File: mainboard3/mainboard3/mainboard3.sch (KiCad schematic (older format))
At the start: 27 parts, among them J0 Conn_01x18, J1 Conn_01x18, J2 Conn_01x18, J4 Conn_01x18, J5 Conn_01x18, T0 Screw_Terminal_01x06, T1 Screw_Terminal_01x06, T10 Screw_Terminal_01x06, T11 Screw_Terminal_01x06, T12 Screw_Terminal_01x06, T2 Screw_Terminal_01x06, T3 Screw_Terminal_01x06, T4 Screw_Terminal_01x06, T5 Screw_Terminal_01x06, T6 Screw_Terminal_01x06, T7 Screw_Terminal_01x06, T8 Screw_Terminal_01x06, T9 Screw_Terminal_01x06, U1 STM32_F4xx, U2 ModuleINA3221, U3 ModuleINA3221, U4 ModuleINA3221, U5 ModuleINA3221, U6 ULN2803A, U7 ULN2803A, X1 Screw_Terminal_01x04

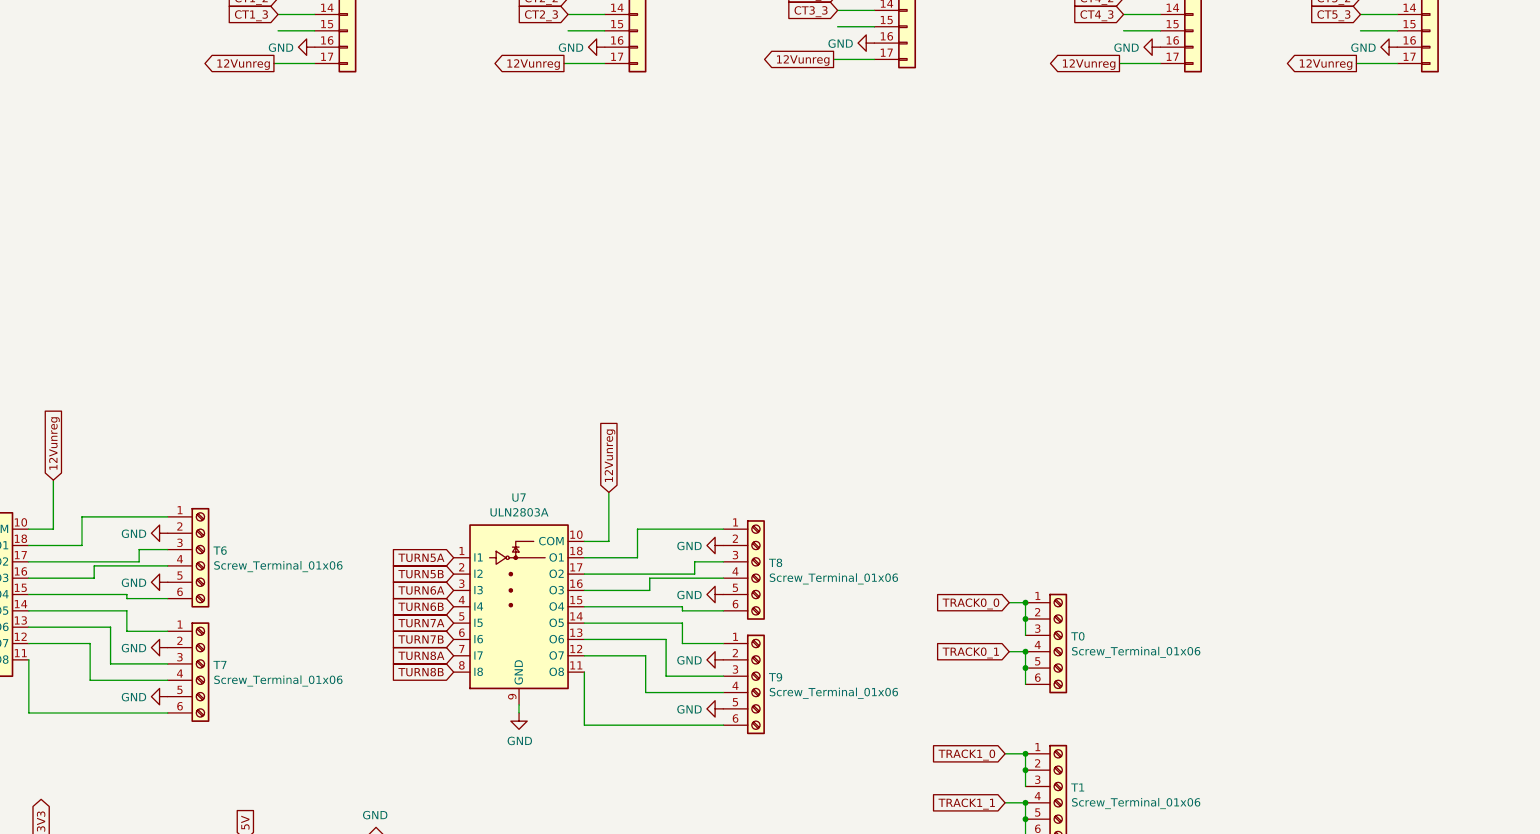
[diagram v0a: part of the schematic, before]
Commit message: adding CAN interface
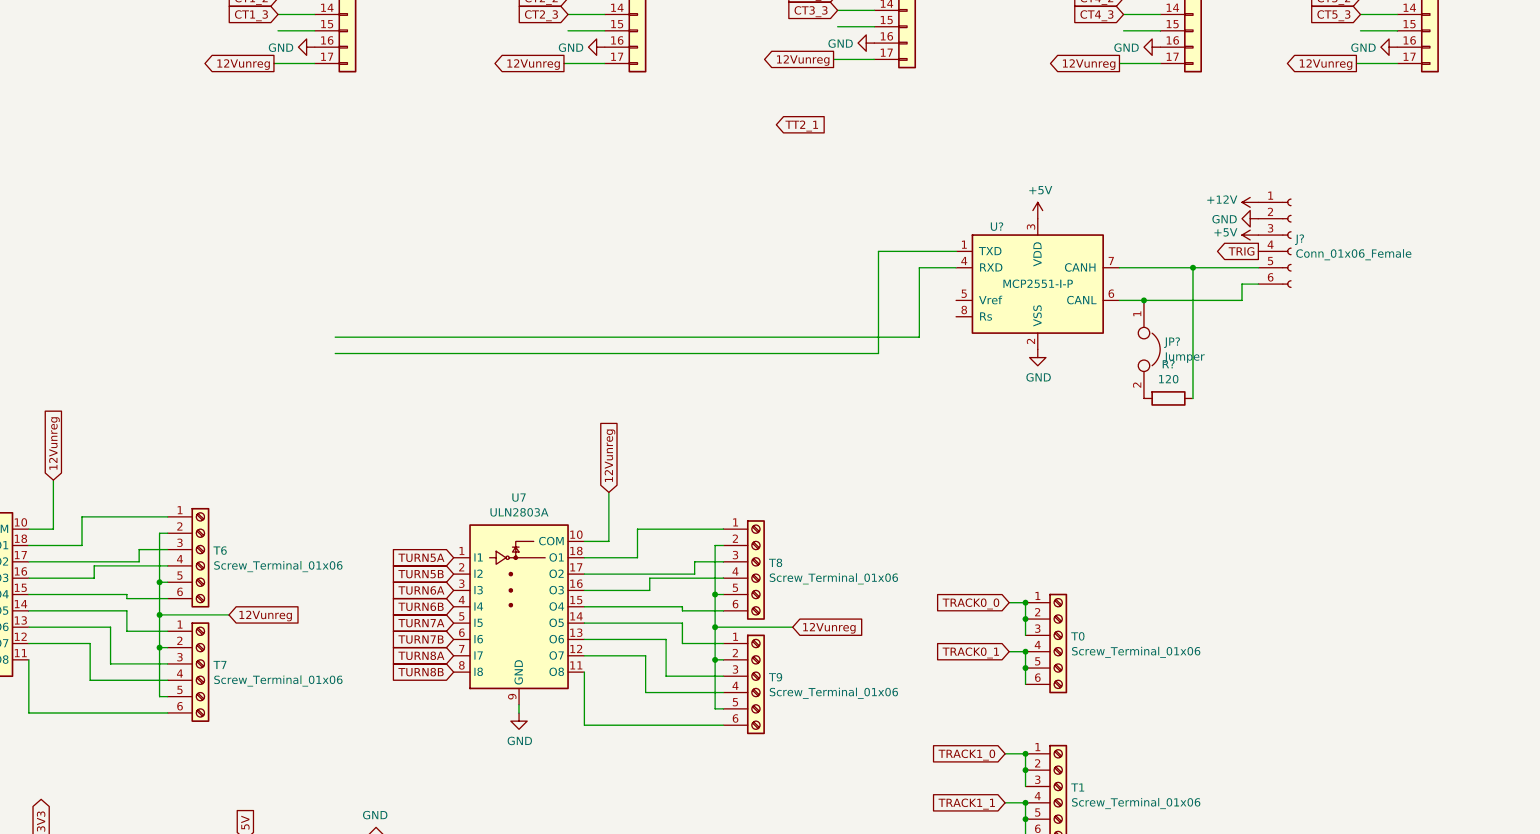
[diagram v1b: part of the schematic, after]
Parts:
- added J?: Conn_01x06_Female, Connector_PinHeader_2.54mm:PinHeader_1x06_P2.54mm_Vertical, symbol Connector:Conn_01x06_Female
- added JP?: Jumper, Connector_PinHeader_2.54mm:PinHeader_1x02_P2.54mm_Vertical, symbol Device:Jumper
- added R?: 120, Resistor_THT:R_Axial_DIN0207_L6.3mm_D2.5mm_P7.62mm_Horizontal, symbol Device:R
- added U?: MCP2551-I-P, Package_DIP:DIP-8_W7.62mm, symbol Interface_CAN_LIN:MCP2551-I-P
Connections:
- net labels added: +12V, +5V, TRIG, TT2_1
- wire segments 201 -> 232
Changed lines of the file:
@@
 Wire Wire Line
 	2350 6550 2350 6225
-$Comp
-L power:GND #PWR0112
-U 1 1 60F13817
-P 3200 5450
-F 0 "#PWR0112" H 3200 5200 50  0001 C CNN
-F 1 "GND" V 3205 5322 50  0000 R CNN
-F 2 "" H 3200 5450 50  0001 C CNN
-F 3 "" H 3200 5450 50  0001 C CNN
-	1    3200 5450
-	0    1    1    0
-$EndComp
-$Comp
-L power:GND #PWR0113
-U 1 1 60F13F45
-P 3200 5750
-F 0 "#PWR0113" H 3200 5500 50  0001 C CNN
-F 1 "GND" V 3205 5622 50  0000 R CNN
-F 2 "" H 3200 5750 50  0001 C CNN
-F 3 "" H 3200 5750 50  0001 C CNN
-	1    3200 5750
-	0    1    1    0
-$EndComp
-$Comp
-L power:GND #PWR0114
-U 1 1 60F1440A
-P 3200 6150
-F 0 "#PWR0114" H 3200 5900 50  0001 C CNN
-F 1 "GND" V 3205 6022 50  0000 R CNN
-F 2 "" H 3200 6150 50  0001 C CNN
-F 3 "" H 3200 6150 50  0001 C CNN
-	1    3200 6150
-	0    1    1    0
-$EndComp
-$Comp
-L power:GND #PWR0115
-U 1 1 60F14973
-P 3200 6450
-F 0 "#PWR0115" H 3200 6200 50  0001 C CNN
-F 1 "GND" V 3205 6322 50  0000 R CNN
-F 2 "" H 3200 6450 50  0001 C CNN
-F 3 "" H 3200 6450 50  0001 C CNN
-	1    3200 6450
-	0    1    1    0
-$EndComp
 Text GLabel 2500 5125 1    50   Input ~ 0
 12Vunreg
@@
 Wire Wire Line
 	5750 6625 5750 6300
-$Comp
-L power:GND #PWR0118
-U 1 1 6108F63E
-P 6600 5525
-F 0 "#PWR0118" H 6600 5275 50  0001 C CNN
-F 1 "GND" V 6605 5397 50  0000 R CNN
-F 2 "" H 6600 5525 50  0001 C CNN
-F 3 "" H 6600 5525 50  0001 C CNN
-	1    6600 5525
-	0    1    1    0
-$EndComp
-$Comp
-L power:GND #PWR0119
-U 1 1 6108F644
-P 6600 5825
-F 0 "#PWR0119" H 6600 5575 50  0001 C CNN
-F 1 "GND" V 6605 5697 50  0000 R CNN
-F 2 "" H 6600 5825 50  0001 C CNN
-F 3 "" H 6600 5825 50  0001 C CNN
-	1    6600 5825
-	0    1    1    0
-$EndComp
-$Comp
-L power:GND #PWR0120
-U 1 1 6108F64A
-P 6600 6225
-F 0 "#PWR0120" H 6600 5975 50  0001 C CNN
-F 1 "GND" V 6605 6097 50  0000 R CNN
-F 2 "" H 6600 6225 50  0001 C CNN
-F 3 "" H 6600 6225 50  0001 C CNN
-	1    6600 6225
-	0    1    1    0
-$EndComp
-$Comp
-L power:GND #PWR0121
-U 1 1 6108F650
-P 6600 6525
-F 0 "#PWR0121" H 6600 6275 50  0001 C CNN
-F 1 "GND" V 6605 6397 50  0000 R CNN
-F 2 "" H 6600 6525 50  0001 C CNN
-F 3 "" H 6600 6525 50  0001 C CNN
-	1    6600 6525
-	0    1    1    0
-$EndComp
 Text GLabel 5900 5200 1    50   Input ~ 0
 12Vunreg
@@
 Wire Wire Line
 	3950 13825 4200 13825
+Wire Wire Line
+	3150 6150 3200 6150
+Wire Wire Line
+	3150 6150 3150 5950
+Wire Wire Line
+	3150 5750 3200 5750
+Connection ~ 3150 6150
+Wire Wire Line
+	3150 5750 3150 5450
+Wire Wire Line
+	3150 5450 3200 5450
+Connection ~ 3150 5750
+Wire Wire Line
+	3200 6450 3150 6450
+Wire Wire Line
+	3150 6150 3150 6450
+Wire Wire Line
+	3150 5950 3575 5950
+Connection ~ 3150 5950
+Wire Wire Line
+	3150 5950 3150 5750
+Text GLabel 3575 5950 2    50   Input ~ 0
+12Vunreg
+Wire Wire Line
+	6600 5525 6550 5525
+Wire Wire Line
+	6550 5525 6550 5825
+Wire Wire Line
+	6550 5825 6600 5825
+Wire Wire Line
+	6550 5825 6550 6025
+Wire Wire Line
+	6550 6225 6600 6225
+Connection ~ 6550 5825
+Wire Wire Line
+	6550 6225 6550 6525
+Wire Wire Line
+	6550 6525 6600 6525
+Connection ~ 6550 6225
+Wire Wire Line
+	6550 6025 7025 6025
+Connection ~ 6550 6025
+Wire Wire Line
+	6550 6025 6550 6225
+Text GLabel 7025 6025 2    50   Input ~ 0
+12Vunreg
+$Comp
+L Interface_CAN_LIN:MCP2551-I-P U?
+U 1 1 61B9B58C
+P 8525 3925
+F 0 "U?" H 8275 4275 50  0000 C CNN
+F 1 "MCP2551-I-P" H 8525 3925 50  0000 C CNN
+F 2 "Package_DIP:DIP-8_W7.62mm" H 8525 3425 50  0001 C CIN
+F 3 "http://ww1.microchip.com/downloads/en/devicedoc/21667d.pdf" H 8525 3925 50  0001 C CNN
+	1    8525 3925
+	1    0    0    -1
+$EndComp
+$Comp
+L Device:Jumper JP?
+U 1 1 61B9B592
+P 9175 4325
+F 0 "JP?" V 9129 4452 50  0000 L CNN
+F 1 "Jumper" V 9220 4452 50  0000 L CNN
+F 2 "Connector_PinHeader_2.54mm:PinHeader_1x02_P2.54mm_Vertical" H 9175 4325 50  0001 C CNN
+F 3 "~" H 9175 4325 50  0001 C CNN
+	1    9175 4325
+	0    1    1    0
+$EndComp
+$Comp
+L Device:R R?
+U 1 1 61B9B598
+P 9325 4625
+F 0 "R?" V 9118 4625 50  0000 C CNN
+F 1 "120" V 9209 4625 50  0000 C CNN
+F 2 "Resistor_THT:R_Axial_DIN0207_L6.3mm_D2.5mm_P7.62mm_Horizontal" V 9255 4625 50  0001 C CNN
+F 3 "~" H 9325 4625 50  0001 C CNN
+	1    9325 4625
+	0    1    1    0
+$EndComp
+Wire Wire Line
+	9025 4025 9175 4025
+Connection ~ 9175 4025
+Wire Wire Line
+	9025 3825 9475 3825
+Connection ~ 9475 3825
+$Comp
+L power:GND #PWR?
+U 1 1 61B9B5A2
+P 8525 4325
+F 0 "#PWR?" H 8525 4075 50  0001 C CNN
+F 1 "GND" H 8530 4152 50  0000 C CNN
+F 2 "" H 8525 4325 50  0001 C CNN
+F 3 "" H 8525 4325 50  0001 C CNN
+	1    8525 4325
+	1    0    0    -1
+$EndComp
+Wire Wire Line
+	9475 3825 9475 4625
+$Comp
+L power:+5V #PWR?
+U 1 1 61B9B5A9
+P 8525 3525
+F 0 "#PWR?" H 8525 3375 50  0001 C CNN
+F 1 "+5V" H 8540 3698 50  0000 C CNN
+F 2 "" H 8525 3525 50  0001 C CNN
+F 3 "" H 8525 3525 50  0001 C CNN
+	1    8525 3525
+	1    0    0    -1
+$EndComp
+Wire Wire Line
+	9475 3825 9875 3825
+Wire Wire Line
+	9875 3925 9775 3925
+Wire Wire Line
+	9775 3925 9775 4025
+Wire Wire Line
+	9175 4025 9775 4025
+$Comp
+L power:GND #PWR?
+U 1 1 61B9B5B3
+P 9875 3525
+F 0 "#PWR?" H 9875 3275 50  0001 C CNN
+F 1 "GND" V 9880 3397 50  0000 R CNN
+F 2 "" H 9875 3525 50  0001 C CNN
+F 3 "" H 9875 3525 50  0001 C CNN
+	1    9875 3525
+	0    1    1    0
+$EndComp
+$Comp
+L power:+5V #PWR?
+U 1 1 61B9B5B9
+P 9875 3625
+F 0 "#PWR?" H 9875 3475 50  0001 C CNN
+F 1 "+5V" V 9890 3753 50  0000 L CNN
+F 2 "" H 9875 3625 50  0001 C CNN
+F 3 "" H 9875 3625 50  0001 C CNN
+	1    9875 3625
+	0    -1   -1   0
+$EndComp
+$Comp
+L Connector:Conn_01x06_Female J?
+U 1 1 61B9B5BF
+P 10075 3625
+F 0 "J?" H 10103 3601 50  0000 L CNN
+F 1 "Conn_01x06_Female" H 10103 3510 50  0000 L CNN
+F 2 "Connector_PinHeader_2.54mm:PinHeader_1x06_P2.54mm_Vertical" H 10075 3625 50  0001 C CNN
+F 3 "~" H 10075 3625 50  0001 C CNN
+	1    10075 3625
+	1    0    0    -1
+$EndComp
+$Comp
+L power:+12V #PWR?
+U 1 1 61B9B5C5
+P 9875 3425
+F 0 "#PWR?" H 9875 3275 50  0001 C CNN
+F 1 "+12V" V 9890 3553 50  0000 L CNN
+F 2 "" H 9875 3425 50  0001 C CNN
+F 3 "" H 9875 3425 50  0001 C CNN
+	1    9875 3425
+	0    -1   -1   0
+$EndComp
+Text GLabel 9875 3725 0    50   Output ~ 0
+TRIG
+Text GLabel 6925 2950 2    50   Input ~ 0
+TT2_1
+Wire Wire Line
+	4225 4350 7550 4350
+Wire Wire Line
+	7550 4350 7550 3725
+Wire Wire Line
+	7550 3725 8025 3725
+Wire Wire Line
+	4225 4250 7800 4250
+Wire Wire Line
+	7800 4250 7800 3825
+Wire Wire Line
+	7800 3825 8025 3825
 $EndSCHEMATC

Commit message: mainboard3 again
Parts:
- removed T0, T1, T12, T2, T3, T4: Screw_Terminal_01x06, Connector_PinHeader_2.54mm:PinHeader_1x06_P2.54mm_Vertical, symbol Connector:Screw_Terminal_01x06
- added 10k1, R1, R20, R21, R22, R23, R24, R25, R26, R27: R, Resistor_THT:R_Axial_DIN0207_L6.3mm_D2.5mm_P7.62mm_Horizontal, symbol Device:R
- added C1, C2, C3, C4, C5: 100nF, Capacitor_THT:C_Disc_D3.4mm_W2.1mm_P2.50mm, symbol Device:C
- added C6: 0.1µF, Capacitor_THT:C_Disc_D3.4mm_W2.1mm_P2.50mm, symbol Device:CP
- added C7: 10µF, Capacitor_THT:CP_Radial_Tantal_D5.0mm_P2.50mm, symbol Device:CP
- added J7: Conn_01x02_Female, Connector_PinHeader_2.54mm:PinHeader_1x02_P2.54mm_Vertical, symbol Connector:Conn_01x02_Female
- added JG2, JG3, JG4, JG5: Conn_01x03_Female, Connector_PinHeader_2.54mm:PinHeader_1x03_P2.54mm_Vertical, symbol Connector:Conn_01x03_Female
- added JI2, JI3, JI4, JI5: Conn_01x06_Female, Connector_PinHeader_2.54mm:PinHeader_1x06_P2.54mm_Vertical, symbol Connector:Conn_01x06_Female
- added JLED1, JLED2: Conn_01x08_Female, Connector_PinHeader_2.54mm:PinHeader_1x08_P2.54mm_Vertical, symbol Connector:Conn_01x08_Female
- added JT_0_1, JT_0_2, JT_0_3, JT_1_1, JT_1_2, JT_1_3, JT_2_1, JT_2_2, JT_3_1, JT_3_2, JT_4_1, JT_5_1: Screw_Terminal_01x02, Connector_PinHeader_2.54mm:PinHeader_1x02_P2.54mm_Vertical, symbol Connector:Screw_Terminal_01x02
- added R10, R11, R12, R13, R14, R15, R16, R17, R18, R19, R3, R4, R5, R6, R7, R8, R9: 10k, Resistor_THT:R_Axial_DIN0207_L6.3mm_D2.5mm_P7.62mm_Horizontal, symbol Device:R
- added R28: 510, Resistor_THT:R_Axial_DIN0207_L6.3mm_D2.5mm_P7.62mm_Horizontal, symbol Device:R
- added R29: 200, Resistor_THT:R_Axial_DIN0207_L6.3mm_D2.5mm_P7.62mm_Horizontal, symbol Device:R
- added R30: 240, Resistor_THT:R_Axial_DIN0207_L6.3mm_D2.5mm_P7.62mm_Horizontal, symbol Device:R
- added SW1: SW_DIP_x01, Connector_PinHeader_2.54mm:PinHeader_1x02_P2.54mm_Vertical, symbol Switch:SW_DIP_x01
- added U10: LM317_TO220, Package_TO_SOT_THT:TO-220-3_Vertical, symbol Regulator_Linear:LM317_TO-220
- added U9: ULN2803A, Package_DIP:DIP-18_W7.62mm, symbol Transistor_Array:ULN2803A
- gave numbers to parts that had none: 4
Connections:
- net labels added: BOARD_LED, BOARD_LED2, CAN_RX, CAN_TX, I10A, I10B, I11A, I11B, I12A, I12B, I1A, I1B, I2A, I2B, I3A, I3B, I4A, I4B, I5A, I5B, I6A, I6B, I7A, I7B, I8A, I8B, I9A, I9B, LED3, LED4, LED5, LED6, LED7, LED8, V5
- wire segments 232 -> 353
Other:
- moved on the sheet: U3, U4, U5

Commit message: mainboard3  routing
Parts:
- removed JLED1, JLED2: Conn_01x08_Female, Connector_PinHeader_2.54mm:PinHeader_1x08_P2.54mm_Vertical, symbol Connector:Conn_01x08_Female
- removed R25, R26, R27: R, Resistor_THT:R_Axial_DIN0207_L6.3mm_D2.5mm_P7.62mm_Horizontal, symbol Device:R
- removed T6, T7, T8, T9: Screw_Terminal_01x06, Connector_PinHeader_2.54mm:PinHeader_1x06_P2.54mm_Vertical, symbol Connector:Screw_Terminal_01x06
- added J?: Conn_02x05_Odd_Even, symbol Connector_Generic:Conn_02x05_Odd_Even
- added J_T1, J_T2, J_T3, J_T4, J_T5, J_T6, J_T7: Conn_01x03_Female, Connector_PinHeader_2.54mm:PinHeader_1x03_P2.54mm_Vertical, symbol Connector:Conn_01x03_Female
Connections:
- net labels removed: LED6, LED7, LED8, TURN8A
- wire segments 353 -> 337
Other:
- moved on the sheet: R20, R21, R22, R23, R24

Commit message: before moving to kicad6
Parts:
- removed J6: Conn_01x06_Female, Connector_PinHeader_2.54mm:PinHeader_1x06_P2.54mm_Vertical, symbol Connector:Conn_01x06_Female
- added C8: 0.1µF, Capacitor_THT:C_Disc_D3.4mm_W2.1mm_P2.50mm, symbol Device:CP
- added C9: 10µF, Capacitor_THT:CP_Radial_Tantal_D5.0mm_P2.50mm, symbol Device:CP
- added J_BUS1, J_GUI1: Conn_01x05_Female, Connector_PinHeader_2.54mm:PinHeader_1x05_P2.54mm_Vertical, symbol Connector:Conn_01x05_Female
- added R25, R26: R, Resistor_THT:R_Axial_DIN0207_L6.3mm_D2.5mm_P7.62mm_Horizontal, symbol Device:R
- added R27: 240, Resistor_THT:R_Axial_DIN0207_L6.3mm_D2.5mm_P7.62mm_Horizontal, symbol Device:R
- added SW2, SW3: SW_DIP_x01, Connector_PinHeader_2.54mm:PinHeader_1x02_P2.54mm_Vertical, symbol Switch:SW_DIP_x01
- added U11: LM317_TO220, Package_TO_SOT_THT:TO-220-3_Vertical, symbol Regulator_Linear:LM317_TO-220
- J8: renamed from J?; footprint (none) -> Connector_PinHeader_2.54mm:PinHeader_2x05_P2.54mm_Vertical
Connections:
- net labels added: 12V
- net labels removed: +12V, +5V, TRIG, TT2_1, V5
- wire segments 337 -> 365
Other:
- moved on the sheet: C6, C7, J7, R28, R29, R30, SW1, U10
